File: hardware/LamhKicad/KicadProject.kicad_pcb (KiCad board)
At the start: 2 copper layers, 5 parts, among them U1 TJA1051T-3, U2 PCA9745BTW, U3 TLV70433DBVT, U4 INA180A3, U5 STM32F072C8Tx

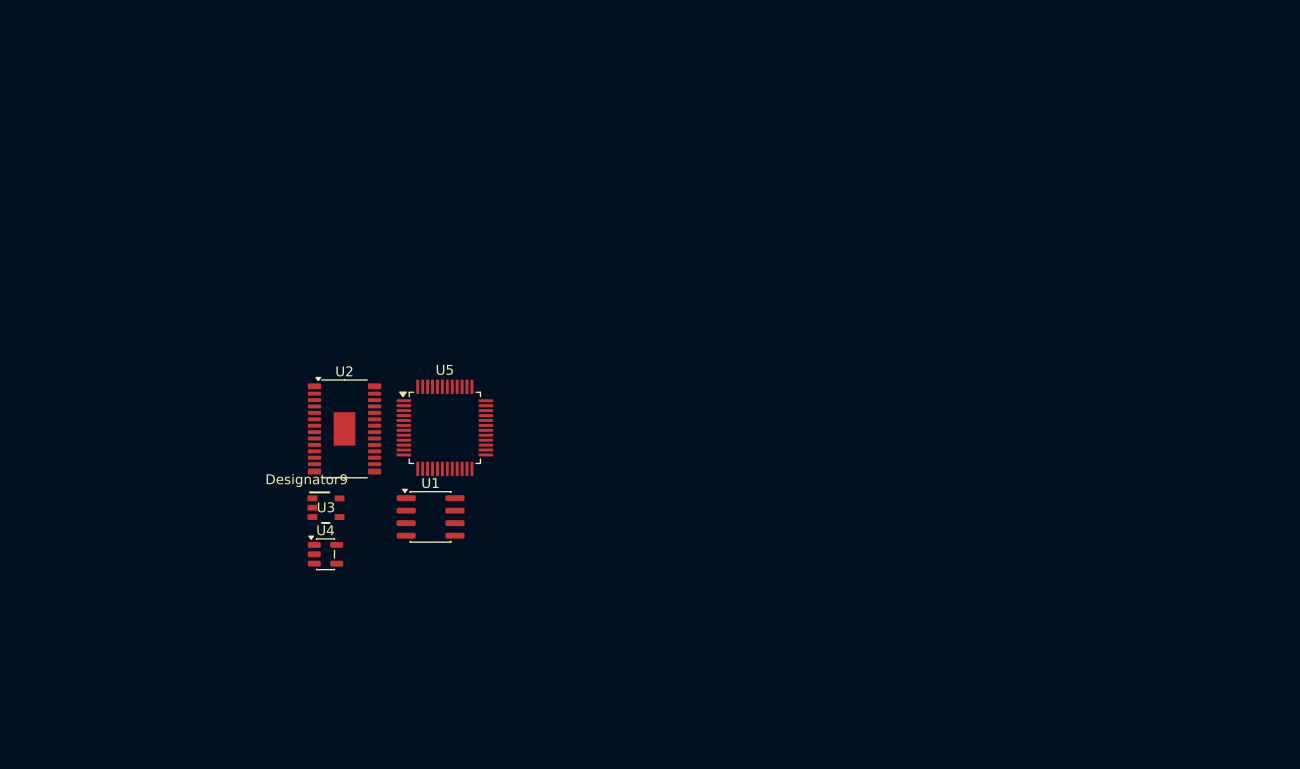
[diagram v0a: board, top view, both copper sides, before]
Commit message: Some fixes to PCB editor conversion
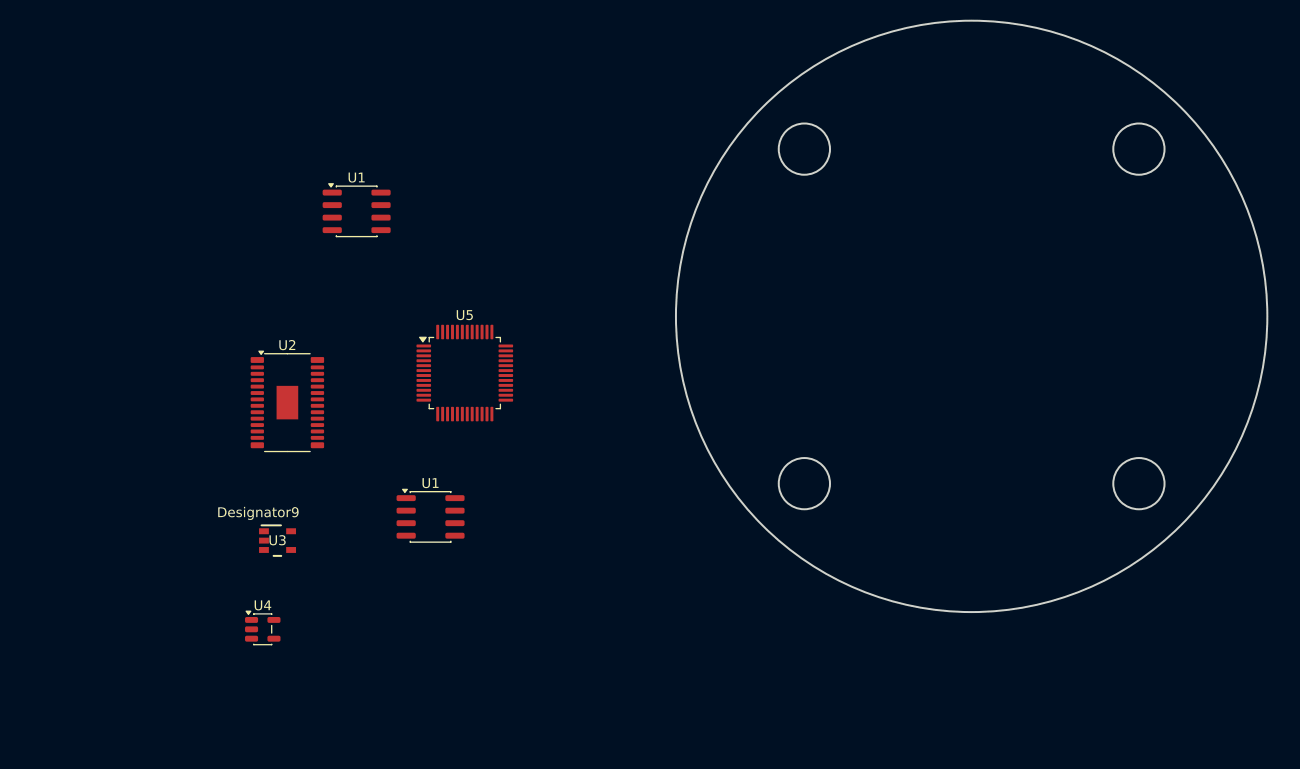
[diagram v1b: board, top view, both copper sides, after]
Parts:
- added U1: TJA1051T-3, Package_SO:SOIC-8_3.9x4.9mm_P1.27mm, F.Cu at (127.0, 85.6)
- moved U4 9.92 mm to (117.5, 128.0)
- moved U2 6.38 mm to (120.0, 105.0)
- moved U3 5.94 mm to (119.0, 119.0)
- moved U5 5.92 mm to (138.0, 102.0)
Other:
- board outline added: 60 x 60 mm

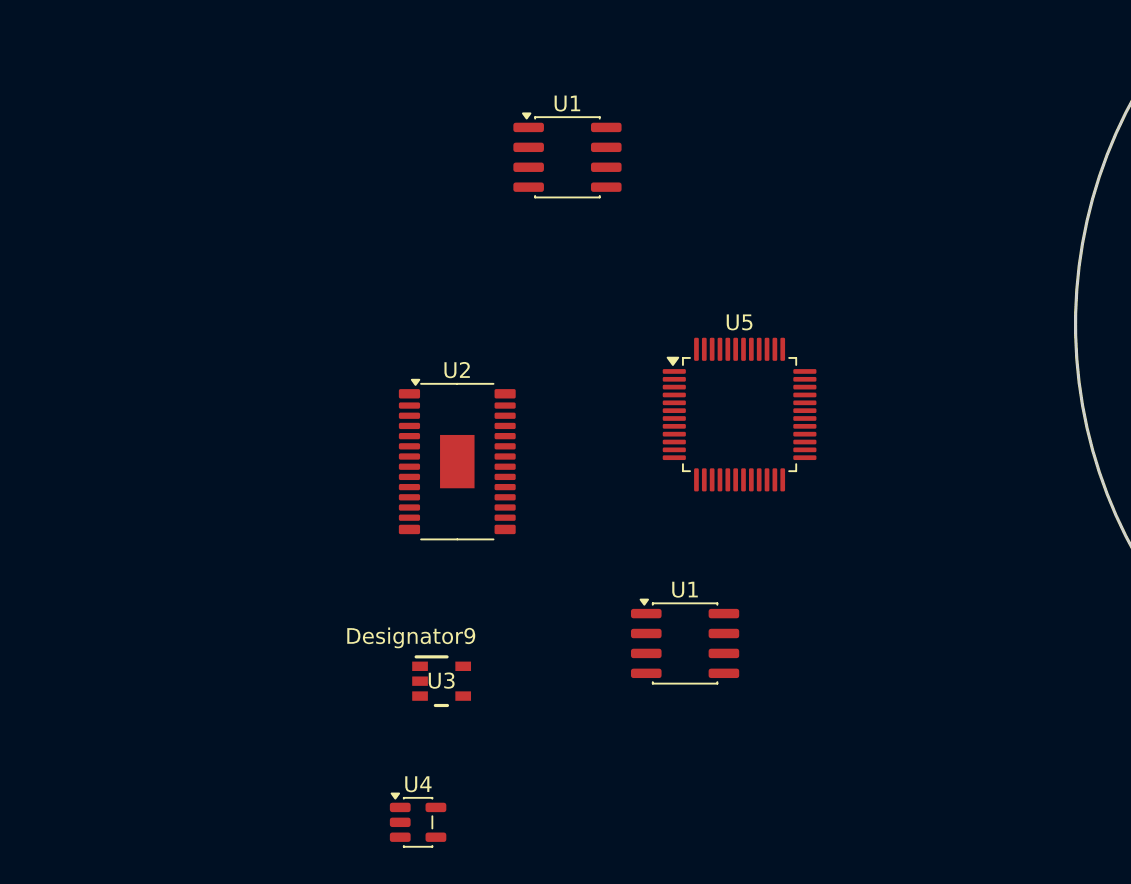
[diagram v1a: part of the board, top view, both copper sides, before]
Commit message: Fixed all footprints
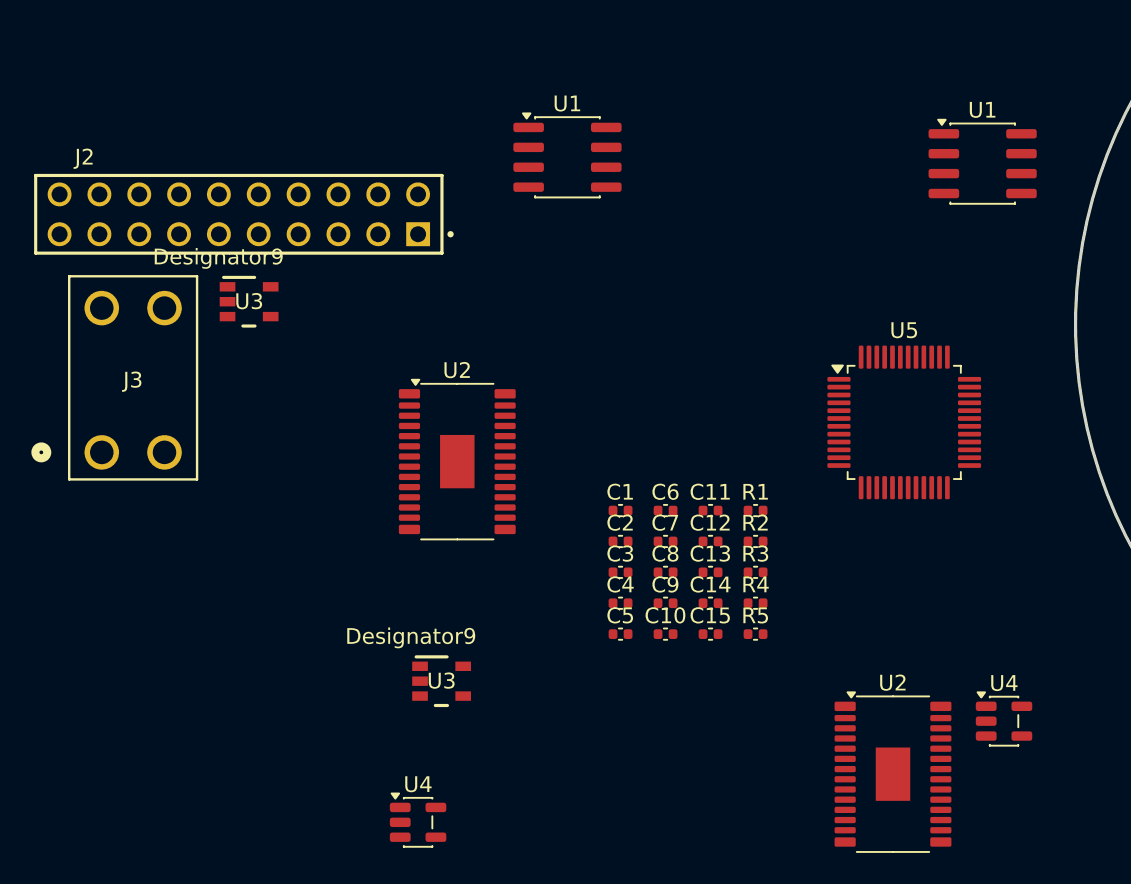
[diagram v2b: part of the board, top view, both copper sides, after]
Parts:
- added C1: 100nF, Capacitor_SMD:C_0402_1005Metric, F.Cu at (130.4, 108.1)
- added C10: 100 nF, Capacitor_SMD:C_0402_1005Metric, F.Cu at (133.3, 116.0)
- added C11: 100 nF, Capacitor_SMD:C_0402_1005Metric, F.Cu at (136.2, 108.1)
- added C12: 1uF, Capacitor_SMD:C_0402_1005Metric, F.Cu at (136.2, 110.1)
- added C13: 10nF, Capacitor_SMD:C_0402_1005Metric, F.Cu at (136.2, 112.1)
- added C14: 4.7 uF, Capacitor_SMD:C_0402_1005Metric, F.Cu at (136.2, 114.0)
- added C15: 100 nF, Capacitor_SMD:C_0402_1005Metric, F.Cu at (136.2, 116.0)
- added C2: 100nF, Capacitor_SMD:C_0402_1005Metric, F.Cu at (130.4, 110.1)
- added C3: 47 uF, Capacitor_SMD:C_0402_1005Metric, F.Cu at (130.4, 112.1)
- added C4: 100nF, Capacitor_SMD:C_0402_1005Metric, F.Cu at (130.4, 114.0)
- added C5: 100uF, Capacitor_SMD:C_0402_1005Metric, F.Cu at (130.4, 116.0)
- added C6: 47 uF, Capacitor_SMD:C_0402_1005Metric, F.Cu at (133.3, 108.1)
- added C7: 4.7 uF, Capacitor_SMD:C_0402_1005Metric, F.Cu at (133.3, 110.1)
- added C8: 100 nF, Capacitor_SMD:C_0402_1005Metric, F.Cu at (133.3, 112.1)
- added C9: 100 nF, Capacitor_SMD:C_0402_1005Metric, F.Cu at (133.3, 114.0)
- added J2: ESQ-110-X-X-D, footprints:SAMTEC_ESQ-110-14-G-D, F.Cu at (106.1, 89.2)
- added J3: 2060-1452/998-404, footprints:WAG, F.Cu at (97.3, 104.4)
- added R1: 10kΩ, Capacitor_SMD:C_0402_1005Metric, F.Cu at (139.0, 108.1)
- added R2: ISET, Capacitor_SMD:C_0402_1005Metric, F.Cu at (139.0, 110.1)
- added R3: 10kΩ, Capacitor_SMD:C_0402_1005Metric, F.Cu at (139.0, 112.1)
- added R4: 60 Ω, Capacitor_SMD:C_0402_1005Metric, F.Cu at (139.0, 114.0)
- added R5: 60 Ω, Capacitor_SMD:C_0402_1005Metric, F.Cu at (139.0, 116.0)
- added U2: PCA9745BTW, Package_SO:NXP_HTSSOP-28-1EP_4.4x9.7mm_P0.65mm_EP2.2x3.4mm, F.Cu at (147.8, 124.9)
- added U3: TLV70433DBVT, footprints:DBV0005A_N, F.Cu at (106.7, 94.8)
- added U4: INA180A3, Package_TO_SOT_SMD:SOT-23-5, F.Cu at (154.9, 121.5)
- moved U1 36.0 mm to (153.5, 86.0)
- moved U5 10.5 mm to (148.5, 102.5)

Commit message: Changes
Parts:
- removed J3: 2060-1452/998-404, footprints:WAG
- removed R1, R3: 10kΩ, Capacitor_SMD:C_0402_1005Metric
- removed R2: ISET, Capacitor_SMD:C_0402_1005Metric
- removed the U1 at (153.5, 86.0)
- removed the U2 at (120.0, 105.0)
- removed the U2 at (147.8, 124.9)
- removed the U3 at (119.0, 119.0)
- removed the U4 at (117.5, 128.0)
- removed the U4 at (154.9, 121.5)
- added D1: NUP2105L, Package_TO_SOT_SMD:SOT-23, F.Cu at (208.1, 104.0)
- added J1: Conn_02x03_Odd_Even, Connector_PinHeader_1.00mm:PinHeader_2x03_P1.00mm_Vertical, F.Cu at (125.0, 137.5)
- added U2: PCA9685PW_112, footprints:TSSOP28_SOT361-1_NXP, F.Cu at (155.5, 129.3)
- J2: moved to B.Cu
- R4, R5: footprint Capacitor_SMD:C_0402_1005Metric -> Resistor_SMD:R_0402_1005Metric
- moved J2 108.1 mm to (213.9, 96.3), turned to 90 degrees
- moved U3 100.2 mm to (206.6, 87.5), turned to 180 degrees
- moved C5 84.6 mm to (209.5, 86.0), turned to -90 degrees
- moved C2 82.1 mm to (209.5, 88.0), turned to -90 degrees
- moved U1 70.9 mm to (195.5, 104.1)
- moved C6 70.8 mm to (204.0, 104.0)
- moved R4 65.9 mm to (204.0, 103.0), turned to 180 degrees
- moved R5 65.9 mm to (204.0, 105.0)
- moved C10 44.6 mm to (175.4, 101.3), turned to 180 degrees
- moved C9 44.3 mm to (175.4, 100.2), turned to 180 degrees
- moved C8 44.0 mm to (175.4, 99.2), turned to 180 degrees
- moved C7 43.8 mm to (175.4, 98.1), turned to 180 degrees
- moved C11 39.6 mm to (175.4, 102.3), turned to 180 degrees
- moved C13 33.8 mm to (168.4, 102.0)
- moved C14 33.8 mm to (168.4, 104.0)
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- renumbered U5 to U4
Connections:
- C2 pad 1: 5VSERVO -> 5VLOGIC
- C5 pad 2: +3.3V -> 3.3V
- J2 pad 13: unconnected-(J2-Pad13) -> GND
- J2 pad 15: CAN_lo -> GND
- J2 pad 18: GND -> CAN_lo
- R4 pad 1: CAN_hi -> CAN_+
- R5 pad 2: CAN_lo -> CAN_-
- U1 pad 1: CAN_TX -> CAN_+
- U1 pad 4: CAN_RX -> CAN_-
- U1 pad 6: CAN_lo -> CAN_-
- U1 pad 7: CAN_hi -> CAN_+
- U3 pad 2: 5VSERVO -> 5VLOGIC
- U3 pad 3: +3.3V -> 3.3V
- U4 pad 32: CAN_RX -> CAN_-
- U4 pad 33: CAN_TX -> CAN_+
- U4 pad 39: DROGUE_FIRE -> unconnected-(U4-PB3-Pad39)
- U4 pad 40: MAIN_FIRE -> unconnected-(U4-PB4-Pad40)
- U4 pad 41: AUX1_FIRE -> unconnected-(U4-PB5-Pad41)
- U4 pad 42: AUX2_FIRE -> unconnected-(U4-PB6-Pad42)
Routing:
- net CAN_+: track 0.00 -> 19.3 mm
- net CAN_-: track 0.00 -> 18.4 mm
- net 3.3V: track 0.00 -> 7.30 mm
- net GND: track 0.00 -> 5.81 mm
- net 5VLOGIC: track 0.00 -> 1.52 mm

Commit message: cleaning up
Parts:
- removed J2: ESQ-110-X-X-D, footprints:SAMTEC_ESQ-110-14-G-D
- added J5: ESQ-110-X-X-D, footprints:SAMTEC_ESQ-110-14-G-D, F.Cu at (213.9, 96.2)
- J1: value Conn_02x03_Odd_Even -> JTAG-10 PIN; footprint Connector_PinHeader_1.00mm:PinHeader_2x03_P1.00mm_Vertical -> Connector_IDC:IDC-Header_2x05_P2.54mm_Vertical
- moved C1 85.8 mm to (215.7, 117.9)
- moved C3 85.8 mm to (215.7, 121.8)
- moved C4 85.8 mm to (215.7, 123.8)
- moved J1 61.8 mm to (184.4, 120.4), turned to 90 degrees
- moved C12 54.9 mm to (220.0, 119.3)
- moved C13 54.9 mm to (220.0, 120.8)
- moved C14 54.9 mm to (220.0, 122.8)
- moved C15 54.9 mm to (220.0, 124.8)
- moved U2 50.4 mm to (189.5, 92.0)
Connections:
- net NRST renamed NRST4
- J1 pad 2: SWDIO -> SWCLK
- J1 pad 3: GND -> unconnected-(J1-Pin_3-Pad3)
- J1 pad 4: SWCLK -> SWDIO
- J1 pad 6: 3.3V_Dig -> GND

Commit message: progs, yes
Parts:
- added C17: 10uF, Capacitor_SMD:C_0402_1005Metric, F.Cu at (193.6, 93.9)
- added J2: 436500303, footprints:MOLEX_436500303, F.Cu at (167.8, 92.2)
- added J3: 436500303, footprints:MOLEX_436500303, F.Cu at (167.8, 106.2)
- added J4: 436500303, footprints:MOLEX_436500303, F.Cu at (192.0, 76.1)
- added J6: 436500303, footprints:MOLEX_436500303, F.Cu at (178.2, 75.9)
- added JP1: SolderJumper_2_Open, Jumper:SolderJumper-2_P1.3mm_Open_TrianglePad1.0x1.5mm, F.Cu at (196.8, 88.0)
- added JP2: SolderJumper_2_Open, Jumper:SolderJumper-2_P1.3mm_Open_TrianglePad1.0x1.5mm, F.Cu at (200.2, 89.0)
- added JP3: SolderJumper_2_Open, Jumper:SolderJumper-2_P1.3mm_Open_TrianglePad1.0x1.5mm, F.Cu at (196.7, 91.0)
- added JP4: SolderJumper_2_Open, Jumper:SolderJumper-2_P1.3mm_Open_TrianglePad1.0x1.5mm, F.Cu at (200.2, 91.8)
- added R1: 220Ω, Resistor_SMD:R_0402_1005Metric, F.Cu at (171.2, 92.2)
- added R10: 10kΩ, Resistor_SMD:R_0402_1005Metric, F.Cu at (209.2, 124.0)
- added R11: 10kΩ, Resistor_SMD:R_0402_1005Metric, F.Cu at (189.5, 94.8)
- added R12: 10kΩ, Resistor_SMD:R_0402_1005Metric, F.Cu at (209.2, 128.0)
- added R13: 10kΩ, Resistor_SMD:R_0402_1005Metric, F.Cu at (209.2, 130.0)
- added R2: 220Ω, Resistor_SMD:R_0402_1005Metric, F.Cu at (171.0, 106.2)
- added R3: 220Ω, Resistor_SMD:R_0402_1005Metric, F.Cu at (192.0, 79.5)
- added R6: 220Ω, Resistor_SMD:R_0402_1005Metric, F.Cu at (178.2, 79.2)
- added R7: 4.7kΩ, Resistor_SMD:R_0402_1005Metric, F.Cu at (192.0, 96.5)
- added R8: 4.7kΩ, Resistor_SMD:R_0402_1005Metric, F.Cu at (192.2, 95.5)
- added R9: 10kΩ, Resistor_SMD:R_0402_1005Metric, F.Cu at (209.2, 122.0)
- moved C9 17.3 mm to (192.7, 101.0), turned to -90 degrees
- moved C10 16.2 mm to (189.5, 109.2)
- moved C8 9.25 mm to (184.5, 97.8), turned to 0 degrees
- moved C11 6.24 mm to (181.2, 100.2), turned to 90 degrees
- moved U4 5.67 mm to (187.0, 103.6)
- moved C7 5.31 mm to (180.2, 100.2), turned to 90 degrees
- moved C2 2.74 mm to (208.4, 90.5)
- moved C5 2.74 mm to (208.4, 88.5)
- moved U3 2.74 mm to (205.5, 90.0)
- moved U1 2.25 mm to (197.8, 104.1)
- moved U2 2.18 mm to (188.2, 90.2), turned to -90 degrees
- moved J1 1.35 mm to (183.1, 121.0)
- moved J5 1.16 mm to (212.8, 96.3)
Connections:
- C2 pad 1: 5VLOGIC -> 5V_LOGIC
- U2 pad 1: unconnected-(U2-A0-Pad1) -> Net-(JP1-B)
- U2 pad 14: unconnected-(U2-VSS-Pad14) -> GND
- U2 pad 2: unconnected-(U2-A1-Pad2) -> Net-(JP2-B)
- U2 pad 23: unconnected-(U2-*OE-Pad23) -> Net-(U2-*OE)
- U2 pad 25: unconnected-(U2-EXTCLK-Pad25) -> GND
- U2 pad 26: unconnected-(U2-SCL-Pad26) -> SCL
- U2 pad 27: unconnected-(U2-SDA-Pad27) -> SDA
- U2 pad 28: unconnected-(U2-VDD-Pad28) -> 3.3V
- U2 pad 3: unconnected-(U2-A2-Pad3) -> Net-(JP3-B)
- U2 pad 4: unconnected-(U2-A3-Pad4) -> Net-(JP4-B)
- U2 pad 6: unconnected-(U2-LED0-Pad6) -> Net-(U2-LED0)
- U2 pad 7: unconnected-(U2-LED1-Pad7) -> Net-(U2-LED1)
- U2 pad 8: unconnected-(U2-LED2-Pad8) -> Net-(U2-LED2)
- U2 pad 9: unconnected-(U2-LED3-Pad9) -> Net-(U2-LED3)
- U3 pad 2: 5VLOGIC -> 5V_LOGIC
- U4 pad 21: SCL -> unconnected-(U4-PB10-Pad21)
- U4 pad 22: MAIN_SEAT -> unconnected-(U4-PB11-Pad22)
- U4 pad 25: AUX1_SEAT -> unconnected-(U4-PB12-Pad25)
- U4 pad 26: AUX2_SEAT -> unconnected-(U4-PB13-Pad26)
- U4 pad 27: SCL -> unconnected-(U4-PB14-Pad27)
- U4 pad 43: unconnected-(U4-PB7-Pad43) -> SDA
- U4 pad 45: unconnected-(U4-PB8-Pad45) -> SCL
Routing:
- net CAN_+: track 19.3 -> 4.52 mm
- net CAN_-: track 18.4 -> 3.72 mm
- net 5V_LOGIC: track 0.00 -> 7.19 mm
- net 3.3V: track 7.30 -> 1.53 mm
- net GND: track 5.81 -> 1.56 mm
- net 5VLOGIC: track 1.52 -> 0.00 mm
